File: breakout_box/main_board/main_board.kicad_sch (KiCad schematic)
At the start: 41 parts, among them CN1 19PIN_LEMO, Q1 DMP3099L, Q2 MJD122, Q3 MMBT5401, Q4 DMP3099L

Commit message: Change the component to C2977785, plus various PCB refinements
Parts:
- R7: LCSC C1712932 -> C2977785
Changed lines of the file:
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@@
       (effects (font (size 1.27 1.27)) hide)
     )
-    (property "LCSC" "C1712932" (id 4) (at 194.31 198.12 0)
+    (property "LCSC" "C2977785" (id 4) (at 194.31 198.12 0)
       (effects (font (size 1.27 1.27)) hide)
     )

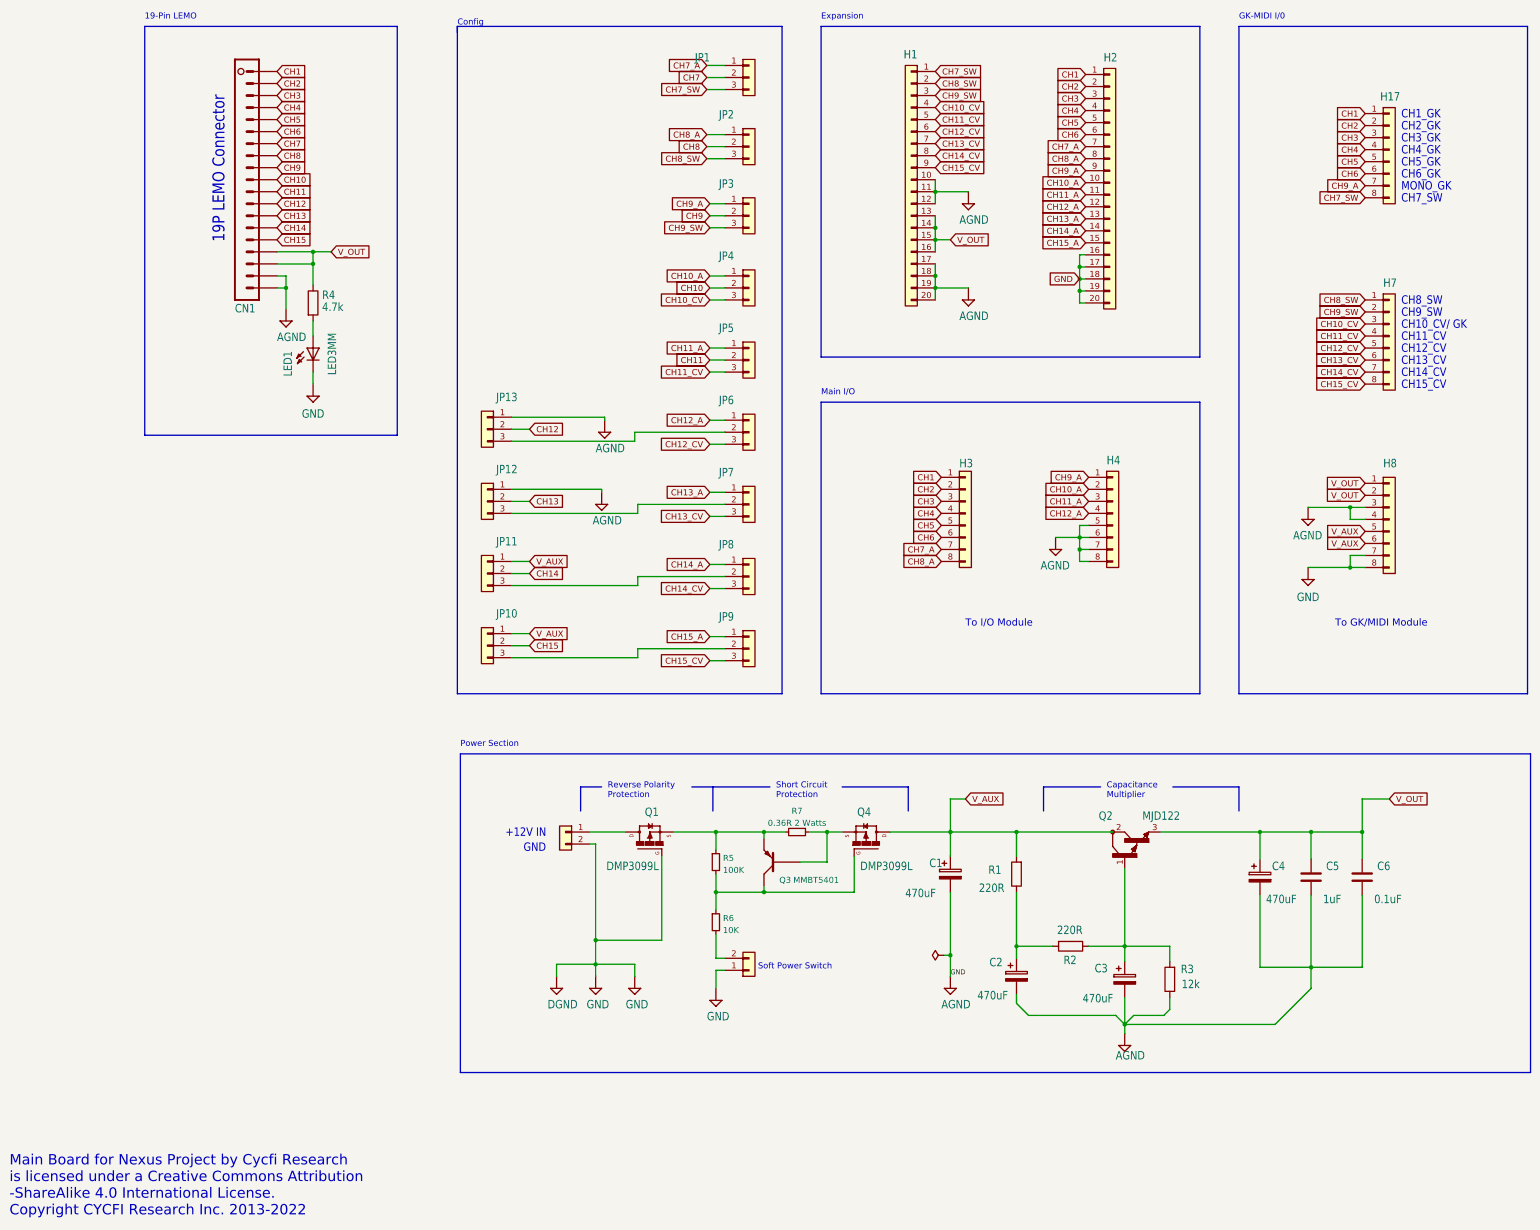
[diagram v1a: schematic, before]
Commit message: Use AOZ1360AIL load switch
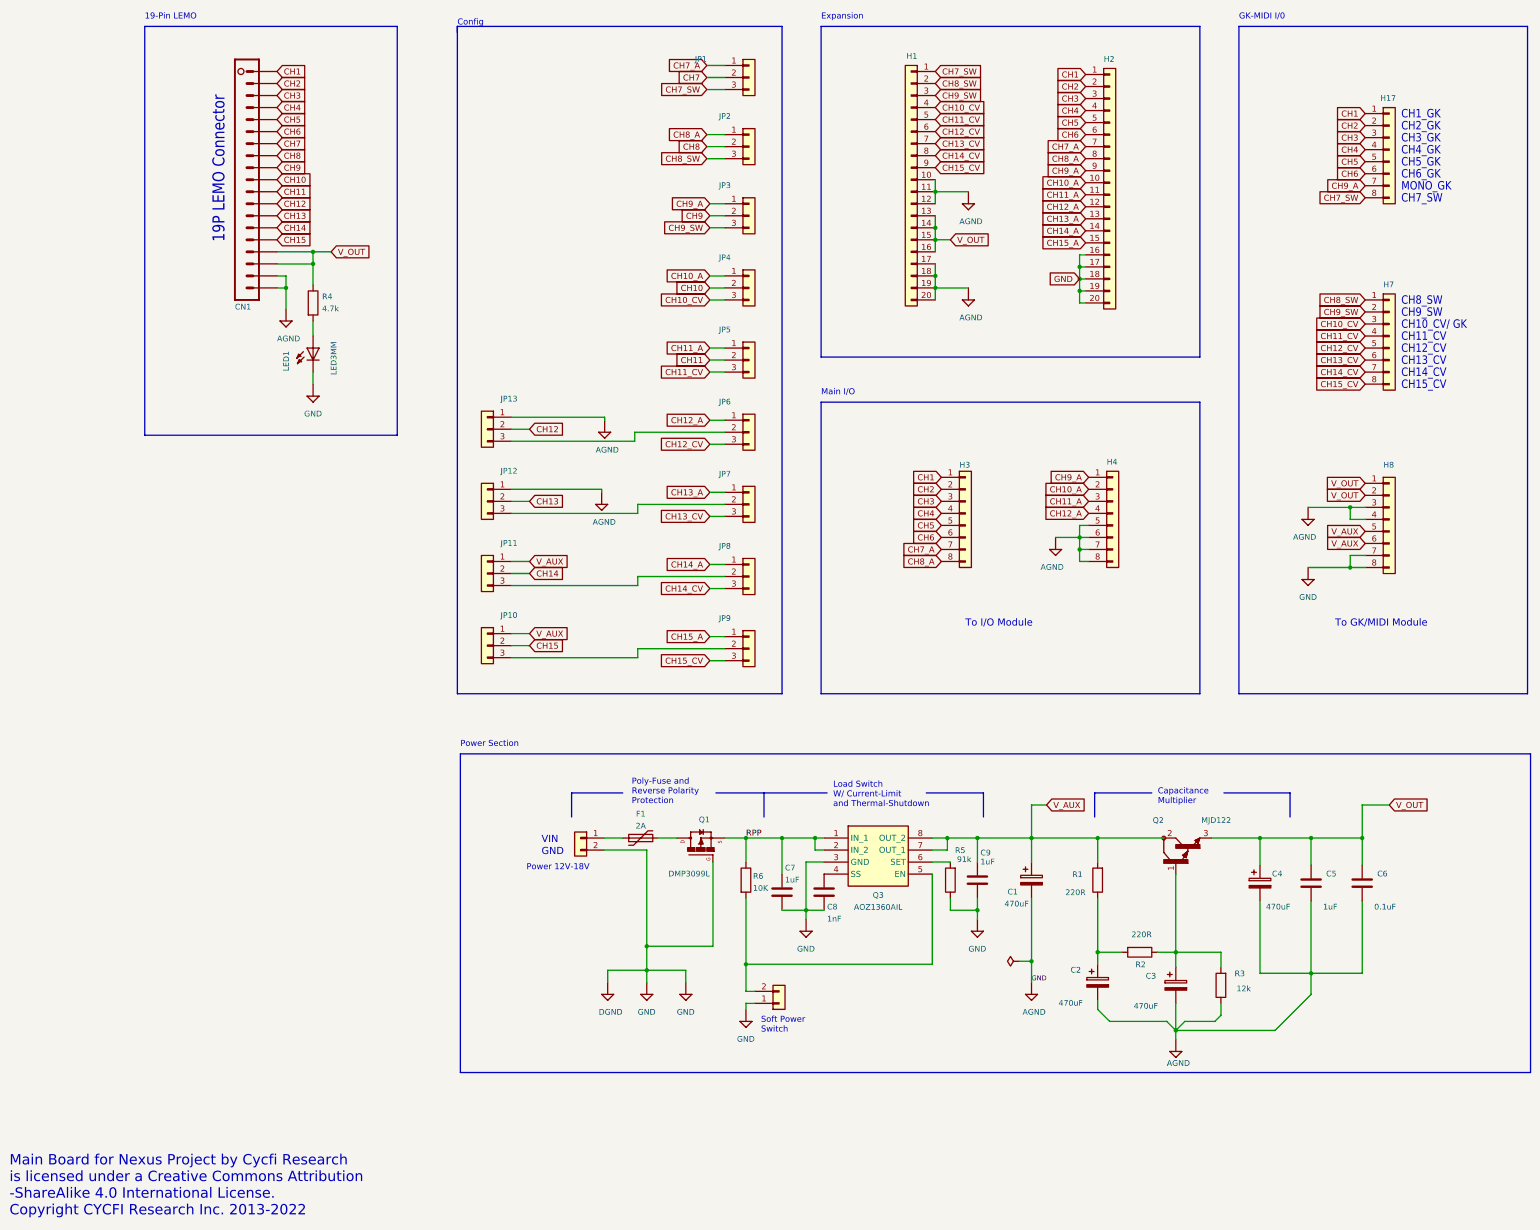
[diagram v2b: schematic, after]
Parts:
- removed Q3: MMBT5401, Package_TO_SOT_SMD:SOT-23, symbol Device:Q_PNP_BEC
- removed Q4: DMP3099L, Package_TO_SOT_SMD:SOT-23, symbol main_board-eagle-import:P_MOSFET
- removed R5: 100K, Resistor_SMD:R_0402_1005Metric, symbol Device:R_Small
- removed R7: 0.36R 2 Watts, Resistor_SMD:R_2512_6332Metric, symbol Device:R_Small
- added C7, C9: 1uF, Capacitor_SMD:C_0603_1608Metric, symbol Device:C
- added C8: 1nF, Capacitor_SMD:C_0402_1005Metric, symbol Device:C
- added F1: 2A, Fuse:Fuse_1812_4532Metric, symbol Device:Polyfuse
- added Q3: AOZ1360AIL, cycfi_library:SOIC127P600X175-8N, symbol cycfi_library:AOZ1360AIL
- added R5: 91k, Resistor_SMD:R_0603_1608Metric, symbol Device:R
- R6: symbol Device:R_Small -> Device:R
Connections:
- net GND: now also C7.2, C8.2, C9.2, Q3.3 (GND), R5.1
- net V_AUX: now also C9.1, Q3.7 (OUT_1), Q3.8 (OUT_2)
- net RPP: now reaches Q1.2 (S)
- net RPP: now also R6.1, C7.1, Q3.1 (IN_1), Q3.2 (IN_2)
- net at H5.2 (Pin_2), R6.2: now also Q3.5 (EN)
- net at H6.1 (Pin_1): now also F1.1; no longer Q1.3 (D)
- new net: F1.2, Q1.3 (D)
- new net: C8.1, Q3.4 (SS)
- new net: Q3.6 (SET), R5.2
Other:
- note added: "Load Switch W/ Current-Limit and Thermal-Shutdown"
- note added: "Poly-Fuse and Reverse Polarity Protection"
- note added: "Power 12V-18V"
- note added: "VIN"
- note removed: "+12V IN"
- note removed: "Reverse Polarity Protection"
- note removed: "Short Circuit Protection"
- moved on the sheet: C1, C2, C3, C4, C5, C6, Q1, Q2, R1, R2, R3, R6

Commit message: Updates for PCBA and panelization
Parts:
- C1, C2, C3, C4, Q1: JLCPCB_CORRECTION (none) -> 0;0;180
- F1: LCSC (none) -> C883157
- Q3: Arrow Part Number AOZ1360AIL -> (none); Arrow Price/Stock https://www.arrow.com/en/products/aoz1360ail/alpha-and-omeg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 -> (none); JLCPCB_CORRECTION (none) -> 0;0;270; LCSC (none) -> C146821
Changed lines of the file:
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@@
       (effects (font (size 1.27 1.27)) (justify left) hide)
     )
-    (property "Datasheet" "~" (id 3) (at 161.29 199.39 0)
+    (property "Datasheet" "https://datasheet.lcsc.com/lcsc/2203021230_BHFUSE-BSMD1812-200-24V_C883157.pdf" (id 3) (at 161.29 199.39 0)
+      (effects (font (size 1.27 1.27)) hide)
+    )
+    (property "LCSC" "C883157" (id 4) (at 161.29 199.39 90)
       (effects (font (size 1.27 1.27)) hide)
     )
@@
       (effects (font (size 1.27 1.27)) (justify left top) hide)
     )
-    (property "Mouser Part Number" "" (id 7) (at 222.885 894.31 0)
-      (effects (font (size 1.27 1.27)) (justify left top) hide)
-    )
-    (property "Mouser Price/Stock" "" (id 8) (at 222.885 994.31 0)
-      (effects (font (size 1.27 1.27)) (justify left top) hide)
-    )
-    (property "Arrow Part Number" "AOZ1360AIL" (id 9) (at 222.885 1094.31 0)
-      (effects (font (size 1.27 1.27)) (justify left top) hide)
-    )
-    (property "Arrow Price/Stock" "https://www.arrow.com/en/products/aoz1360ail/alpha-and-omega-semiconductor?region=europe" (id 10) (at 222.885 1194.31 0)
-      (effects (font (size 1.27 1.27)) (justify left top) hide)
+    (property "LCSC" "C146821" (id 7) (at 196.215 199.39 0)
+      (effects (font (size 1.27 1.27)) hide)
+    )
+    (property "JLCPCB_CORRECTION" "0;0;270" (id 8) (at 196.215 199.39 0)
+      (effects (font (size 1.27 1.27)) hide)
     )
     (pin "1")
@@
       (effects (font (size 1.27 1.27)) hide)
     )
+    (property "JLCPCB_CORRECTION" "0;0;180" (id 5) (at 292.1 208.915 0)
+      (effects (font (size 1.27 1.27)) hide)
+    )
     (pin "1")
     (pin "2")
@@
       (effects (font (size 1.27 1.27)) hide)
     )
+    (property "JLCPCB_CORRECTION" "0;0;180" (id 5) (at 274.32 230.505 0)
+      (effects (font (size 1.27 1.27)) hide)
+    )
     (pin "1")
     (pin "2")
@@
     )
     (property "LCSC" "C249933" (id 4) (at 243.84 208.28 0)
+      (effects (font (size 1.27 1.27)) hide)
+    )
+    (property "JLCPCB_CORRECTION" "0;0;180" (id 5) (at 243.84 208.28 0)
       (effects (font (size 1.27 1.27)) hide)
     )
@@
       (effects (font (size 1.27 1.27)) hide)
     )
+    (property "JLCPCB_CORRECTION" "0;0;180" (id 5) (at 257.81 229.87 0)
+      (effects (font (size 1.27 1.27)) hide)
+    )
     (pin "1")
     (pin "2")
@@
       (effects (font (size 1.27 1.27)) hide)
     )
-    (property "JLCPCB_CORRECTION" "" (id 5) (at 173.99 199.39 90)
-      (effects (font (size 1.27 1.27)) hide)
-    )
+    (property "JLCPCB_CORRECTION" "0;0;180" (id 5) (at 173.99 199.39 90)
+      (effects (font (size 1.27 1.27)) hide)
+    )

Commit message: Production run May 2025
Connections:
- net GND renamed AGND
